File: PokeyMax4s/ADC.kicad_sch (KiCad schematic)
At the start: 6 parts, among them J1 Audio_in

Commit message: PokeyMax 4s fabrication files
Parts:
- J1: now left out of the parts list
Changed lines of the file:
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@@
 		(unit 1)
 		(exclude_from_sim no)
-		(in_bom yes)
+		(in_bom no)
 		(on_board yes)
 		(dnp no)

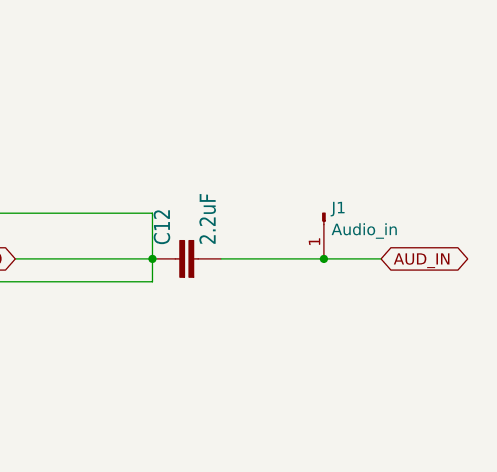
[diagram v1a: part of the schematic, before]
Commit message: Add A4 to PokeyMax 4s
Reroute accordingly
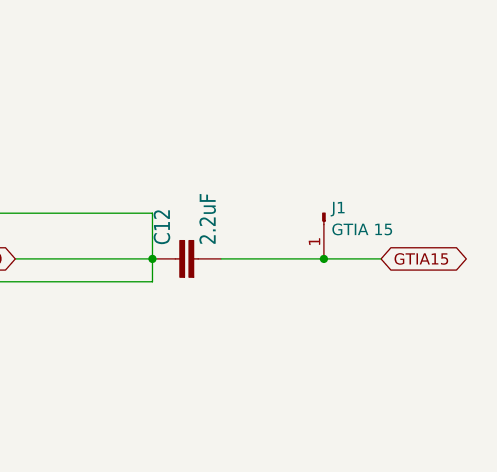
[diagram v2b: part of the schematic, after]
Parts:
- J1: value Audio_in -> GTIA 15
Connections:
- net AUD_IN renamed GTIA15
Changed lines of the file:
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@@
 		)
 	)
-	(global_label "AUD_IN"
+	(global_label "GTIA15"
 		(shape bidirectional)
 		(at 208.28 106.68 0)
@@
 			)
 		)
-		(property "Value" "Audio_in"
+		(property "Value" "GTIA 15"
 			(at 202.7682 103.4471 90)
 			(effects
